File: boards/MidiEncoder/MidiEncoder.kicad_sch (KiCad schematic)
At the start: 12 parts

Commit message: Added Keyboard encoder and Midi encoder design using shift registers
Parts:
- removed J?: MIDI Out, symbol Connector:DIN-5_180degree
- removed R? (x2): 220, Resistor_THT:R_Axial_DIN0204_L3.6mm_D1.6mm_P2.54mm_Vertical, symbol Device:R
- added D?: 1N4148, Diode_THT:D_DO-35_SOD27_P7.62mm_Horizontal, symbol Diode:1N4148
- added J?: Encoder2, symbol Connector_Generic:Conn_02x05_Odd_Even
- added J?: Encoder1, symbol Connector_Generic:Conn_02x05_Odd_Even
- added J?: SelectRX, symbol Connector_Generic:Conn_01x03
- added J?: MIDI In, symbol Connector_Generic:Conn_01x03
- added J?: MIDI Out, symbol Connector_Generic:Conn_01x03
- added R?: 10k, Resistor_THT:R_Axial_DIN0204_L3.6mm_D1.6mm_P2.54mm_Vertical, symbol Device:R
- added R? (x3): 220, Resistor_THT:R_Axial_DIN0204_L3.6mm_D1.6mm_P2.54mm_Vertical, symbol Device:R
- added U?: 6N138, Package_DIP:DIP-8_W7.62mm, symbol Isolator:6N138
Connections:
- net +5V: now also J?.2 (Pin_2), J?.2 (Pin_2), J?.4 (Pin_4), J?.4 (Pin_4), R?.1, R?.2, U?.8 (VCC)
- net GND: now also J?.10 (Pin_10), J?.10 (Pin_10), J?.3 (Pin_3), J?.8 (Pin_8), J?.8 (Pin_8), U?.5 (GND)
- net MISO: now also J?.3 (Pin_3)
- net MOSI: now also J?.9 (Pin_9)
- net RXD: now also J?.2 (Pin_2); no longer J?.3 (Pin_3)
- net SCK: now also J?.5 (Pin_5)
- net TXD: now also R?.1
- net at U?.10 (XTAL2/PB7): now also J?.9 (Pin_9)
- net PL: now reaches U?.23 (PC0)
- net PL: now also J?.6 (Pin_6), J?.6 (Pin_6)
- net CP: now reaches U?.24 (PC1)
- net CP: now also J?.1 (Pin_1), J?.1 (Pin_1)
- net at U?.9 (XTAL1/PB6): now also J?.7 (Pin_7)
- net L1: no longer names the net of U?.14 (PB0)
- net L1: now also J?.3 (Pin_3)
- net L2: no longer names the net of U?.15 (PB1)
- net L2: now also J?.5 (Pin_5)
- net L3: no longer names the net of U?.16 (PB2)
- net L3: now also J?.7 (Pin_7)
- new net: D?.1 (K), R?.2, U?.2 (C1)
- new net: D?.2 (A), J?.2 (Pin_2), U?.3 (C2)
- new net: J?.3 (Pin_3), J?.3 (Pin_3)
- new net: J?.1 (Pin_1), R?.1 (x2)
- new net: J?.2 (Pin_2), R?.2
- new net MIDI Rx: J?.1 (Pin_1), R?.2, U?.6 (VO2)
- no-connect marks 8 -> 12
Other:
- moved on the sheet: C?, J?, R?

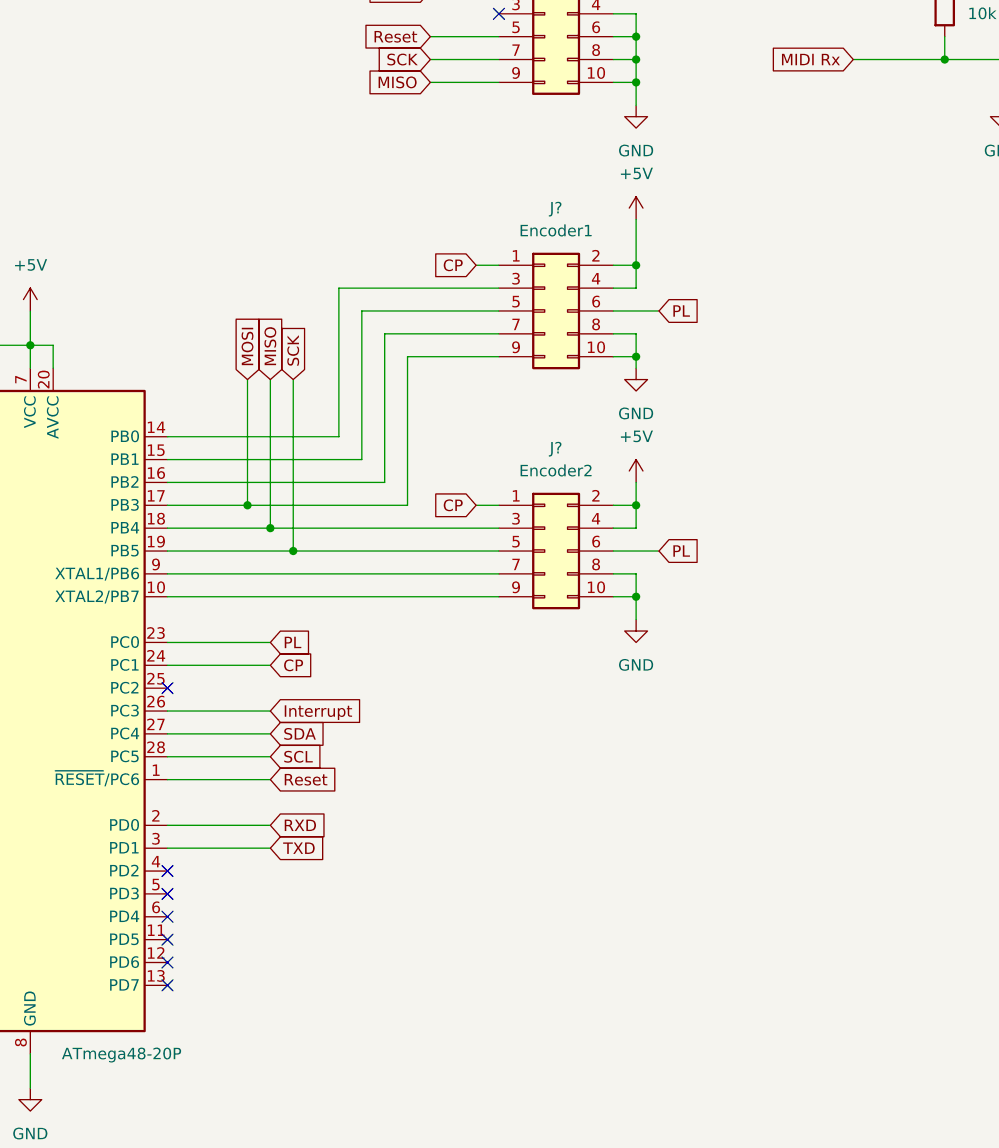
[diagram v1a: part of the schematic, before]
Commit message: Updated keyboard encoder to use 8-1 Mux instead of shift registers
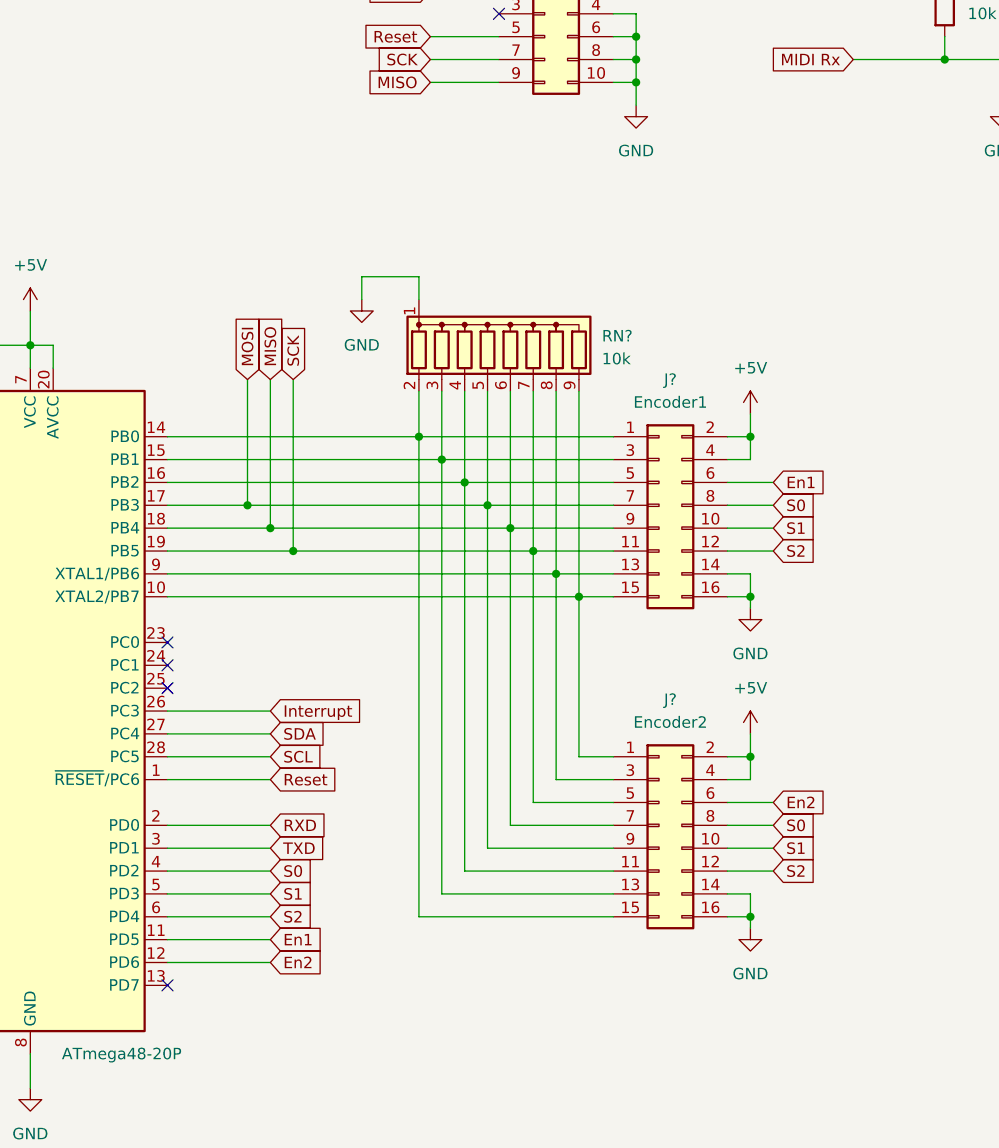
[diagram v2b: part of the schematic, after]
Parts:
- removed J?: Encoder2, symbol Connector_Generic:Conn_02x05_Odd_Even
- removed J?: Encoder1, symbol Connector_Generic:Conn_02x05_Odd_Even
- added J?: Encoder2, symbol Connector_Generic:Conn_02x08_Odd_Even
- added J?: Encoder1, symbol Connector_Generic:Conn_02x08_Odd_Even
- added RN?: 10k, Resistor_THT:R_Array_SIP9, symbol Device:R_Network08
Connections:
- net +5V: now also J?.2 (Pin_2), J?.2 (Pin_2), J?.4 (Pin_4), J?.4 (Pin_4)
- net GND: now also J?.14 (Pin_14), J?.14 (Pin_14), J?.16 (Pin_16), J?.16 (Pin_16), RN?.1 (common)
- net MISO: now also J?.7 (Pin_7), J?.9 (Pin_9), RN?.6 (R5)
- net MOSI: now also J?.7 (Pin_7), J?.9 (Pin_9), RN?.5 (R4)
- net SCK: now also J?.11 (Pin_11), J?.5 (Pin_5), RN?.7 (R6)
- net at U?.9 (XTAL1/PB6): now also J?.13 (Pin_13), J?.3 (Pin_3), RN?.8 (R7)
- net at U?.10 (XTAL2/PB7): now also J?.1 (Pin_1), J?.15 (Pin_15), RN?.9 (R8)
- net at U?.14 (PB0): now also J?.1 (Pin_1), J?.15 (Pin_15), RN?.2 (R1)
- net at U?.15 (PB1): now also J?.13 (Pin_13), J?.3 (Pin_3), RN?.3 (R2)
- net at U?.16 (PB2): now also J?.11 (Pin_11), J?.5 (Pin_5), RN?.4 (R3)
- net En1: now reaches U?.11 (PD5)
- net En1: now also J?.6 (Pin_6)
- net En2: now reaches U?.12 (PD6)
- net En2: now also J?.6 (Pin_6)
- net S0: now reaches U?.4 (PD2)
- net S0: now also J?.8 (Pin_8), J?.8 (Pin_8)
- net S1: now reaches U?.5 (PD3)
- net S1: now also J?.10 (Pin_10), J?.10 (Pin_10)
- net S2: now reaches U?.6 (PD4)
- net S2: now also J?.12 (Pin_12), J?.12 (Pin_12)
- net CP: no longer names the net of U?.24 (PC1)
- net PL: no longer names the net of U?.23 (PC0)
- no-connect marks 12 -> 9

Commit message: Annoted ICs
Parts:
- gave numbers to parts that had none: 21
